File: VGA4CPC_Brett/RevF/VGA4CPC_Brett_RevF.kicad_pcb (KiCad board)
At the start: 2 copper layers, 95 x 76 mm, 51 parts, among them J1 CPC VIDEO IN, J2 LUM OUT, J3 +5V IN, J4 VFREQ, J5 SPARE GPIO, J6 VGA OUT, J7 CPC PLUS VIDEO IN, J8 CPC PLUS AUDIO OUT, SW1 RESET, SW2 WACKED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

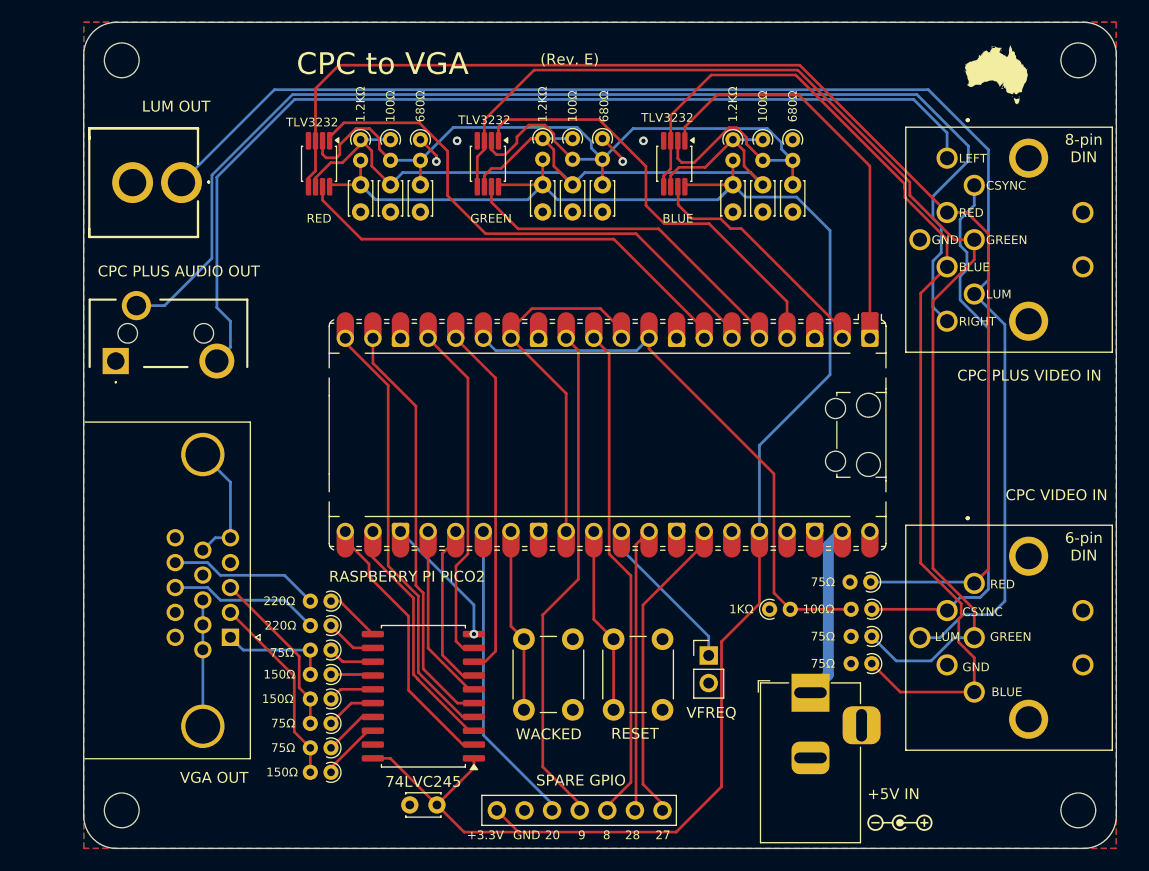
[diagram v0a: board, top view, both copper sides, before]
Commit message: Rev. F initial commit
Moved comparator to own daughterboard
Switched from 3.3V to 5V logic (requires Pico 2 for sure)
Switched 74LVC245 (SMD) to 74HCT245 (through-hole)
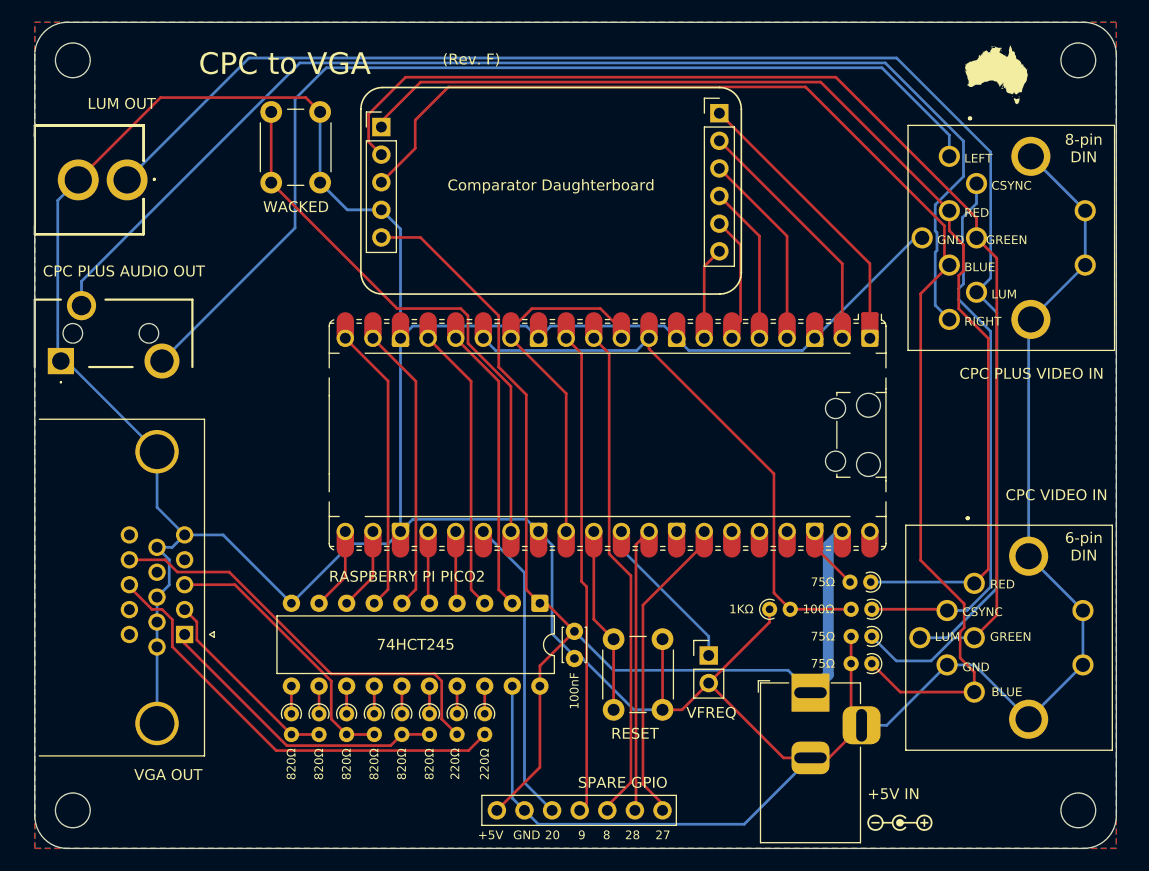
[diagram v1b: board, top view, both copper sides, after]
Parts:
- removed C10, C2, C3, C4, C5, C6, C7, C8, C9: 100nF, Capacitor_THT:C_Disc_D3.0mm_W2.0mm_P2.50mm
- removed R14, R15, R20: 1.2KΩ, Resistor_THT:R_Axial_DIN0204_L3.6mm_D1.6mm_P1.90mm_Vertical
- removed R16, R18, R21: 100Ω, Resistor_THT:R_Axial_DIN0204_L3.6mm_D1.6mm_P1.90mm_Vertical
- removed R17, R19, R22: 680Ω, Resistor_THT:R_Axial_DIN0204_L3.6mm_D1.6mm_P1.90mm_Vertical
- removed U3, U4, U5: TLV3232, Package_SO:VSSOP-8_3x3mm_P0.65mm
- added U6: Comparator Daughterboard, VGA4CPC_Footprints:Comparator Daughterboard, F.Cu at (140.5, 55.2)
- R10, R6, R9: value 150Ω -> 820Ω
- R11, R7, R8: value 75Ω -> 820Ω
- U2: value 74LVC245 -> 74HCT245; footprint Package_SO:SOIC-20W_7.5x12.8mm_P1.27mm -> Package_DIP:DIP-20_W7.62mm
- moved SW2 53.8 mm to (110.7, 65.4)
- moved C1 20.3 mm to (138.6, 109.2), turned to 90 degrees
- moved R12 16.3 mm to (130.3, 114.3), turned to -90 degrees
- moved R13 15.6 mm to (127.8, 114.3), turned to -90 degrees
- moved U2 13.7 mm to (135.4, 104.1), turned to -90 degrees
- moved R10 9.75 mm to (125.2, 114.3), turned to -90 degrees
- moved R11 8.77 mm to (122.7, 114.3), turned to -90 degrees
- moved R6 5.49 mm to (115.1, 114.3), turned to -90 degrees
- moved J8 5.05 mm to (91.3, 81.9)
- moved J2 5.01 mm to (97.4, 65.2)
- moved R7 4.80 mm to (112.5, 114.3), turned to -90 degrees
- moved H3 4.50 mm to (92.4, 54.2)
- moved H4 4.50 mm to (92.4, 123.2)
- moved J6 4.22 mm to (102.7, 107.0)
- moved R8 4.08 mm to (120.1, 114.3), turned to -90 degrees
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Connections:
- C1 pad 2: +3.3V -> +5V
- J5 pad 7: +3.3V -> +5V
- R10 pad 1: Net-(U2-B4) -> Net-(U2-B2)
- R11 pad 1: Net-(U2-B5) -> Net-(U2-B3)
- R12 pad 1: Net-(U2-B6) -> Net-(U2-B0)
- R13 pad 1: Net-(U2-B7) -> Net-(U2-B1)
- R6 pad 1: Net-(U2-B0) -> Net-(U2-B6)
- R7 pad 1: Net-(U2-B1) -> Net-(U2-B7)
- R8 pad 1: Net-(U2-B2) -> Net-(U2-B4)
- R9 pad 1: Net-(U2-B3) -> Net-(U2-B5)
- U1 pad 36: +3.3V -> unconnected-(U1-3V3-Pad36)
- U2 pad 1: +3.3V -> +5V
- U2 pad 2: /VGA_G_{0} -> /VGA_HSYNC
- U2 pad 20: +3.3V -> +5V
- U2 pad 3: /VGA_G_{1} -> /VGA_VSYNC
- U2 pad 4: /VGA_B_{1} -> /VGA_R_{1}
- U2 pad 5: /VGA_B_{0} -> /VGA_R_{0}
- U2 pad 6: /VGA_R_{0} -> /VGA_B_{0}
- U2 pad 7: /VGA_R_{1} -> /VGA_B_{1}
- U2 pad 8: /VGA_HSYNC -> /VGA_G_{1}
- U2 pad 9: /VGA_VSYNC -> /VGA_G_{0}
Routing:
- net GND: track 41.1 -> 419.2 mm, vias 5 -> 0
- net +3.3V: track 167.9 -> 0.00 mm
- net /LOWER: track 90.1 -> 0.00 mm
- net +5V: track 16.0 -> 105.0 mm
- net /UPPER: track 84.5 -> 0.00 mm
- net /R_{0}: track 48.2 -> 10.9 mm
- net Net-(U1-GPIO21): track 16.1 -> 52.0 mm
- net /R_{1}: track 41.3 -> 7.78 mm
- net /VGA_HSYNC_{B}: track 13.9 -> 41.2 mm
- net /VGA_VSYNC_{B}: track 13.9 -> 38.8 mm
- net /G_{0}: track 40.7 -> 17.4 mm
- net /CPC_B: track 96.2 -> 119.3 mm
- net /VGA_R: track 10.1 -> 27.7 mm
- net /G_{1}: track 30.9 -> 13.8 mm
- net /VGA_G_{0}: track 24.3 -> 7.60 mm
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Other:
- board size 95 x 76 mm -> 99.5 x 76 mm
- board text added: "(Rev. F)"
- board text added: "+5V"
- board text added: "B"
- board text added: "G"
- board text added: "INPUT"
- board text added: "OUTPUT"
- board text added: "R"
- board text removed: "(Rev. E)"
- board text removed: "+3.3V"
